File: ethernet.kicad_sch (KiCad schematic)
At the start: 92 parts, among them IC2 ACPL-217-500E, J2 5-2337992-8, U13 TPS2372-3RGWR, U16 TS3L500, U6 KSZ9031RNXCA, Y1 ABM8G-25.000MHZ-18-D2Y-T

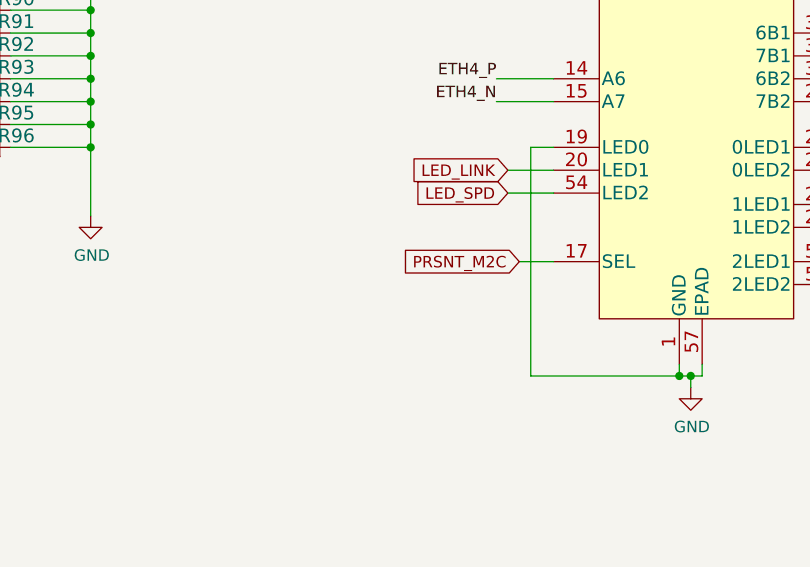
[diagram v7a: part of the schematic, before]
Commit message: Replace MODE2 jumpers with SMD DIP switch. Replace power cycle,VTT_CNTL and SLP_S4 ccircuits with tri-state buffer ones. Add possibilty to swith ETH paths with FPGA
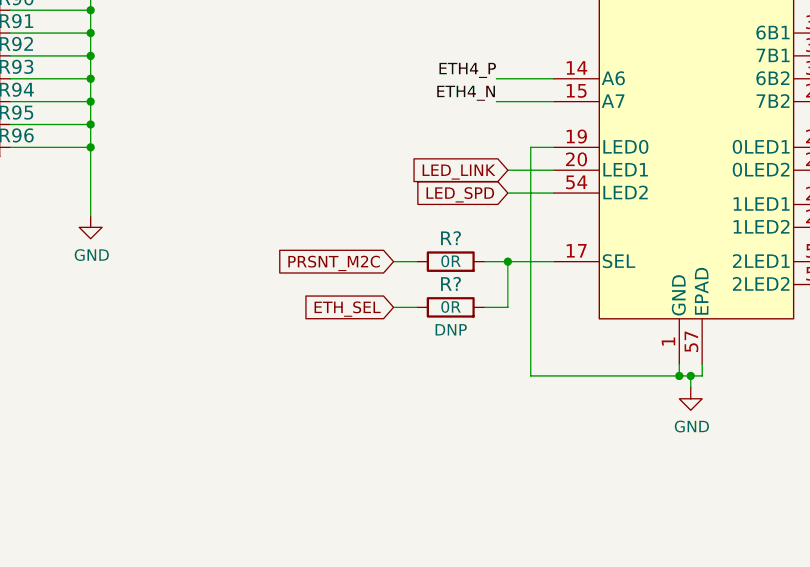
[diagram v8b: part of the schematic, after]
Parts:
- added R? (x2): R_0R_0402, antmicro-footprints:0402-res, symbol antmicroResistors0402:R_0R_0402
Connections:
- net PRSNT_M2C: now also R?.1; no longer U16.17 (SEL)
- new net: R?.2, R?.2, U16.17 (SEL)
- new net ETH_SEL: R?.1
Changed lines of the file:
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@@
   (junction (at 28.575 31.75) (diameter 0) (color 0 0 0 0)
   )
+  (junction (at 339.09 130.81) (diameter 0) (color 0 0 0 0)
+  )
   (junction (at 284.48 199.39) (diameter 0) (color 0 0 0 0)
   )
@@
     (stroke (width 0) (type default) (color 0 0 0 0))
   )
-  (wire (pts (xy 340.36 130.81) (xy 344.17 130.81))
-    (stroke (width 0) (type default) (color 0 0 0 0))
-  )
   (wire (pts (xy 232.41 154.94) (xy 243.84 154.94))
     (stroke (width 0) (type default) (color 0 0 0 0))
@@
     (stroke (width 0) (type default) (color 0 0 0 0))
   )
+  (wire (pts (xy 326.39 130.81) (xy 328.93 130.81))
+    (stroke (width 0) (type default) (color 0 0 0 0))
+  )
   (wire (pts (xy 161.925 108.585) (xy 160.655 108.585))
     (stroke (width 0) (type default) (color 0 0 0 0))
@@
     (stroke (width 0) (type default) (color 0 0 0 0))
   )
+  (wire (pts (xy 326.39 135.89) (xy 328.93 135.89))
+    (stroke (width 0) (type default) (color 0 0 0 0))
+  )
   (wire (pts (xy 284.48 199.39) (xy 284.48 200.66))
     (stroke (width 0) (type default) (color 0 0 0 0))
@@
     (stroke (width 0) (type default) (color 0 0 0 0))
   )
+  (wire (pts (xy 336.55 135.89) (xy 339.09 135.89))
+    (stroke (width 0) (type default) (color 0 0 0 0))
+  )
   (wire (pts (xy 32.385 151.13) (xy 38.735 151.13))
     (stroke (width 0) (type default) (color 0 0 0 0))
@@
     (stroke (width 0) (type default) (color 0 0 0 0))
   )
+  (wire (pts (xy 339.09 130.81) (xy 344.17 130.81))
+    (stroke (width 0) (type default) (color 0 0 0 0))
+  )
   (wire (pts (xy 267.97 54.61) (xy 276.225 54.61))
     (stroke (width 0) (type default) (color 0 0 0 0))
@@
     (stroke (width 0) (type default) (color 0 0 0 0))
   )
+  (wire (pts (xy 339.09 135.89) (xy 339.09 130.81))
+    (stroke (width 0) (type default) (color 0 0 0 0))
+  )
   (wire (pts (xy 283.845 107.95) (xy 292.735 107.95))
     (stroke (width 0) (type default) (color 0 0 0 0))
@@
     (stroke (width 0) (type default) (color 0 0 0 0))
   )
+  (wire (pts (xy 336.55 130.81) (xy 339.09 130.81))
+    (stroke (width 0) (type default) (color 0 0 0 0))
+  )
   (wire (pts (xy 205.105 54.61) (xy 202.565 54.61))
     (stroke (width 0) (type default) (color 0 0 0 0))
@@
     )
   )
-  (global_label "PRSNT_M2C" (shape input) (at 340.36 130.81 180) (fields_autoplaced)
+  (global_label "ETH_SEL" (shape input) (at 326.39 135.89 180) (fields_autoplaced)
     (effects (font (size 1.27 1.27)) (justify right))
-    (property "Intersheet References" "${INTERSHEET_REFS}" (id 0) (at 327.0896 130.7306 0)
+    (property "Intersheet References" "${INTERSHEET_REFS}" (id 0) (at 316.2644 135.8106 0)
+      (effects (font (size 1.27 1.27)) (justify right) hide)
+    )
+  )
+  (global_label "PRSNT_M2C" (shape input) (at 326.39 130.81 180) (fields_autoplaced)
+    (effects (font (size 1.27 1.27)) (justify right))
+    (property "Intersheet References" "${INTERSHEET_REFS}" (id 0) (at 313.1196 130.7306 0)
       (effects (font (size 1.27 1.27)) (justify right) hide)
     )
@@
     (pin "2")
   )
+  (symbol (lib_id "antmicroResistors0402:R_0R_0402") (at 332.74 135.89 0) (unit 1)
+    (in_bom yes) (on_board yes)
+    (property "Reference" "R?" (id 0) (at 332.74 133.35 0)
+      (effects (font (size 1.524 1.524)))
+    )
+    (property "Value" "R_0R_0402" (id 1) (at 332.74 139.7 0)
+      (effects (font (size 1.524 1.524)) hide)
+    )
+    (property "Footprint" "antmicro-footprints:0402-res" (id 2) (at 337.82 130.81 0)
+      (effects (font (size 1.524 1.524)) (justify left) hide)
+    )
+    (property "Datasheet" "" (id 3) (at 332.74 135.89 0)
+      (effects (font (size 1.27 1.27)) hide)
+    )
+    (property "Manufacturer" "PANASONIC" (id 4) (at 337.82 125.73 0)
+      (effects (font (size 1.524 1.524)) (justify left) hide)
+    )
+    (property "MPN" "ERJ2GE0R00X" (id 5) (at 337.82 128.27 0)
+      (effects (font (size 1.524 1.524)) (justify left) hide)
+    )
+    (property "Val" "0R" (id 6) (at 332.74 135.89 0))
+    (property "DNP" "DNP" (id 7) (at 332.74 138.43 0))
+    (pin "1")
+    (pin "2")
+  )
   (symbol (lib_id "data-center-dram-tester:5-2337992-8") (at 7.62 201.295 0) (unit 1)
     (in_bom yes) (on_board yes) (fields_autoplaced)
@@
     (pin "1")
     (pin "2")
+  )
+  (symbol (lib_id "antmicroResistors0402:R_0R_0402") (at 332.74 130.81 0) (unit 1)
+    (in_bom yes) (on_board yes)
+    (property "Reference" "R?" (id 0) (at 332.74 128.27 0)
+      (effects (font (size 1.524 1.524)))
+    )
+    (property "Value" "R_0R_0402" (id 1) (at 332.74 134.62 0)
+      (effects (font (size 1.524 1.524)) hide)
+    )
+    (property "Footprint" "antmicro-footprints:0402-res" (id 2) (at 337.82 125.73 0)
+      (effects (font (size 1.524 1.524)) (justify left) hide)
+    )
+    (property "Datasheet" "" (id 3) (at 332.74 130.81 0)
+      (effects (font (size 1.27 1.27)) hide)
+    )
+    (property "Manufacturer" "PANASONIC" (id 4) (at 337.82 120.65 0)
+      (effects (font (size 1.524 1.524)) (justify left) hide)
+    )
+    (property "MPN" "ERJ2GE0R00X" (id 5) (at 337.82 123.19 0)
+      (effects (font (size 1.524 1.524)) (justify left) hide)
+    )
+    (property "Val" "0R" (id 6) (at 332.74 130.81 0))
+    (pin "1")
+    (pin "2")
